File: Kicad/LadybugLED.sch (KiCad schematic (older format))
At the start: 11 parts

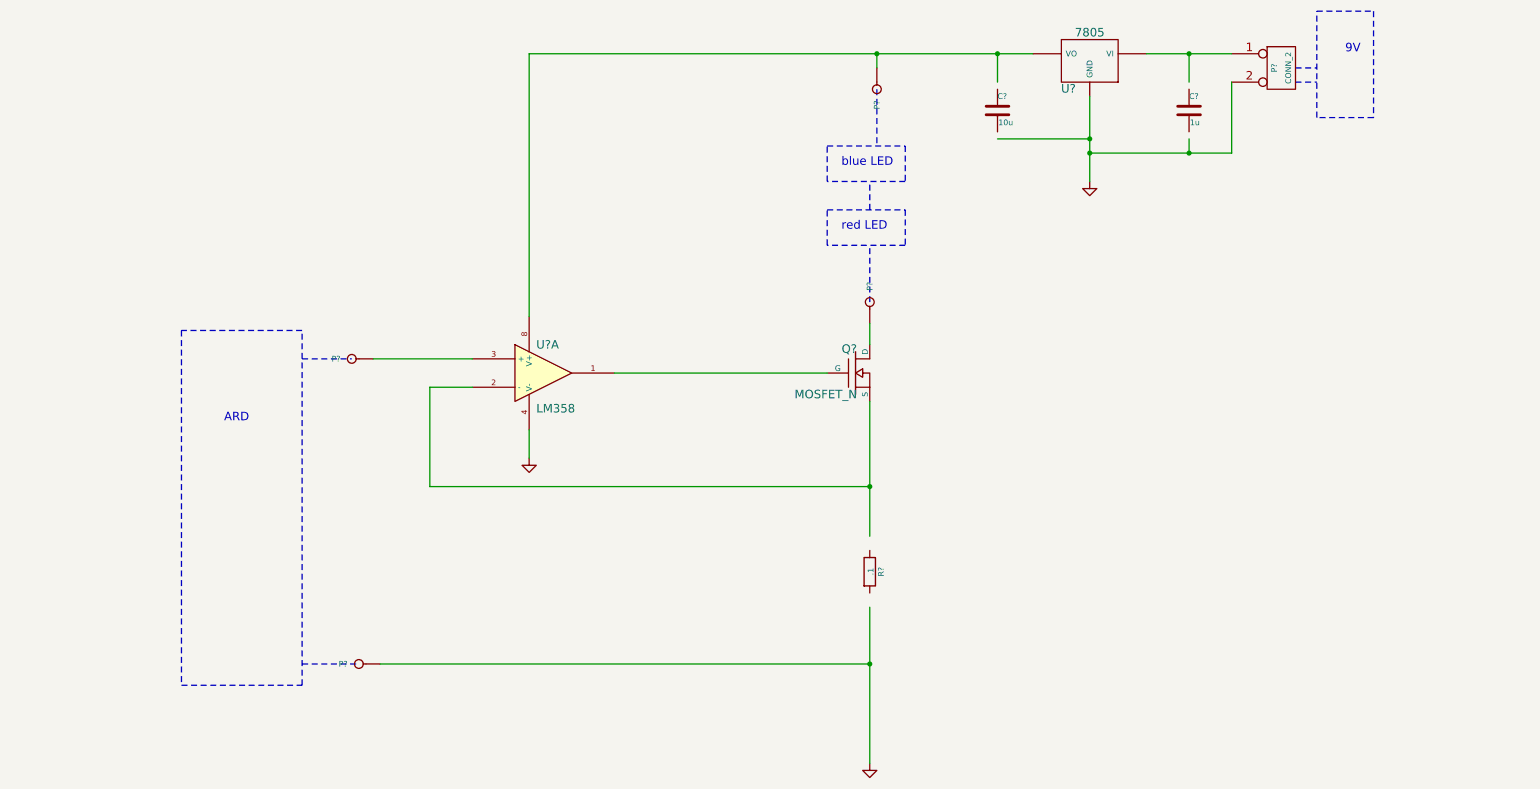
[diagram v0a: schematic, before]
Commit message: added renameGerbers Automator workflow and layout
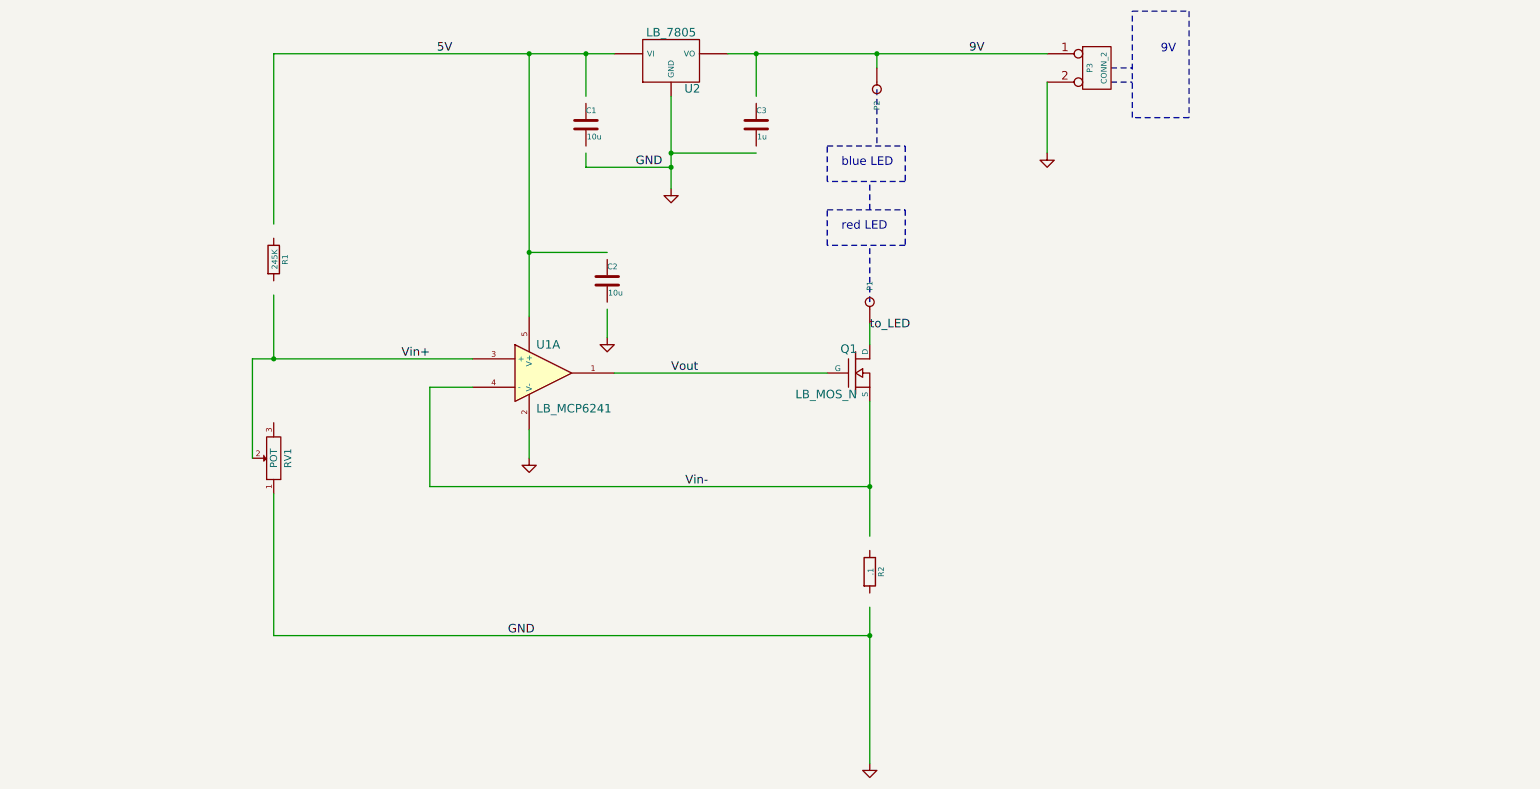
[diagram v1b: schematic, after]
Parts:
- removed C?: 1u, ~, symbol C
- removed C?: 10u, ~, symbol C
- removed P? (x2): CONN_1, symbol CONN_1
- removed Q?: MOSFET_N, ~, symbol MOSFET_N
- removed U?: LM358, symbol LM358
- removed U?: 7805, ~, symbol 7805
- added C1, C2: 10u, ~, symbol C
- added C3: 1u, ~, symbol C
- added Q1: LB_MOS_N, ~, symbol LB_MOS_N
- added R1: 245K, ~, symbol R
- added RV1: POT, ~, symbol POT
- added U1: LB_MCP6241, symbol LB_MCP6241
- added U2: LB_7805, ~, symbol LB_7805
- gave numbers to parts that had none: 4
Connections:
- net labels added: 5V, 9V, Vin+, Vin-, Vout, to_LED
- wire segments 21 -> 27
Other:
- note removed: "ARD"
- moved on the sheet: P3

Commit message: buck regulator LED driver - first commit
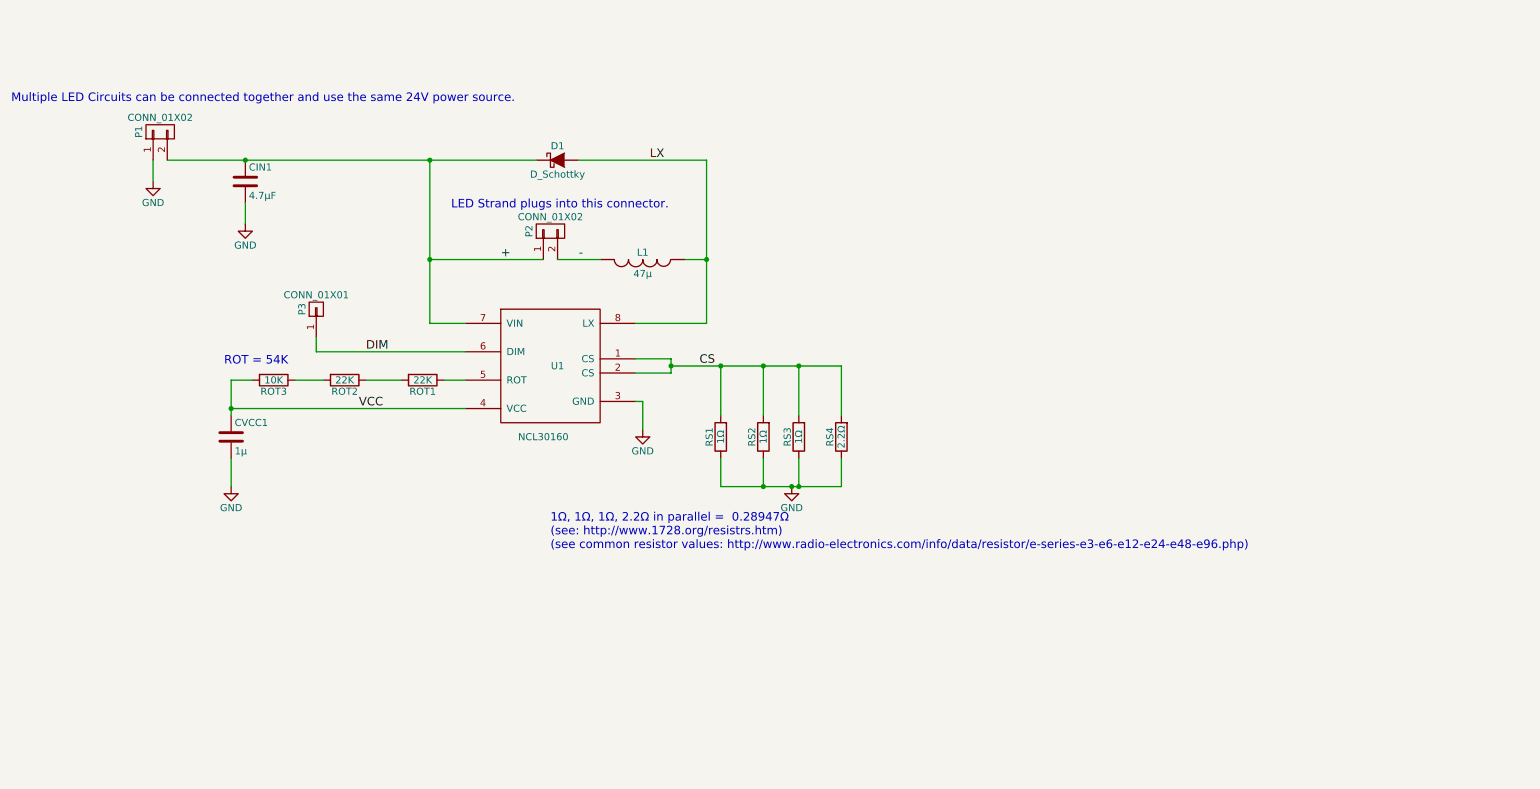
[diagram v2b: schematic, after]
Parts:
- removed C1, C2: 10u, ~, symbol C
- removed C3: 1u, ~, symbol C
- removed P1, P2: CONN_1, symbol CONN_1
- removed P3: CONN_2, symbol CONN_2
- removed Q1: LB_MOS_N, ~, symbol LB_MOS_N
- removed R1: 245K, ~, symbol R
- removed R2: .1, ~, symbol R
- removed RV1: POT, ~, symbol POT
- removed U1: LB_MCP6241, symbol LB_MCP6241
- removed U2: LB_7805, ~, symbol LB_7805
- added CIN1: 4.7µF, Capacitors_SMD:C_0805, symbol C
- added CVCC1: 1µ, Capacitors_SMD:C_0805, symbol C
- added D1: D_Schottky, Diodes_SMD:SOD-123, symbol D_Schottky
- added L1: 47µ, LadybugHydro:L-NR6045T470M, symbol INDUCTOR
- added P1, P2: CONN_01X02, LettuceBuddy:LB_CONN_2, symbol CONN_01X02
- added P3: CONN_01X01, LettuceBuddy:LB_CONN_1, symbol CONN_01X01
- added ROT1, ROT2: 22K, Resistors_SMD:R_0805, symbol R
- added ROT3: 10K, Resistors_SMD:R_0805, symbol R
- added RS1, RS2, RS3: 1Ω, Resistors_SMD:R_0805, symbol R
- added RS4: 2.2Ω, Resistors_SMD:R_0805, symbol R
- added U1: NCL30160, SMD_Packages:SOIC-8-N, symbol NCL30160
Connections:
- net labels added: +, -, CS, DIM, LX, VCC
- net labels removed: 5V, 9V, Vin+, Vin-, Vout, to_LED
- wire segments 27 -> 35
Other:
- note added: "1Ω, 1Ω, 1Ω, 2.2Ω in parallel = 0.28947Ω\n(see: http://www.1728.org/resistrs.htm)\n(see common resistor values: http://www.radio-electronics.com/info/data/resistor/e-series-e3-e6-e12-e24-e48-e96.php)"
- note added: "LED Strand plugs into this connector."
- note added: "Multiple LED Circuits can be connected together and use the same 24V power source."
- note added: "ROT = 54K"
- note removed: "9V"
- note removed: "blue LED\n"
- note removed: "red LED\n"
